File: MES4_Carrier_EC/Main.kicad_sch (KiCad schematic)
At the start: 20 parts, among them J1 2199230-3, J2 STDC14, SW1 RESET

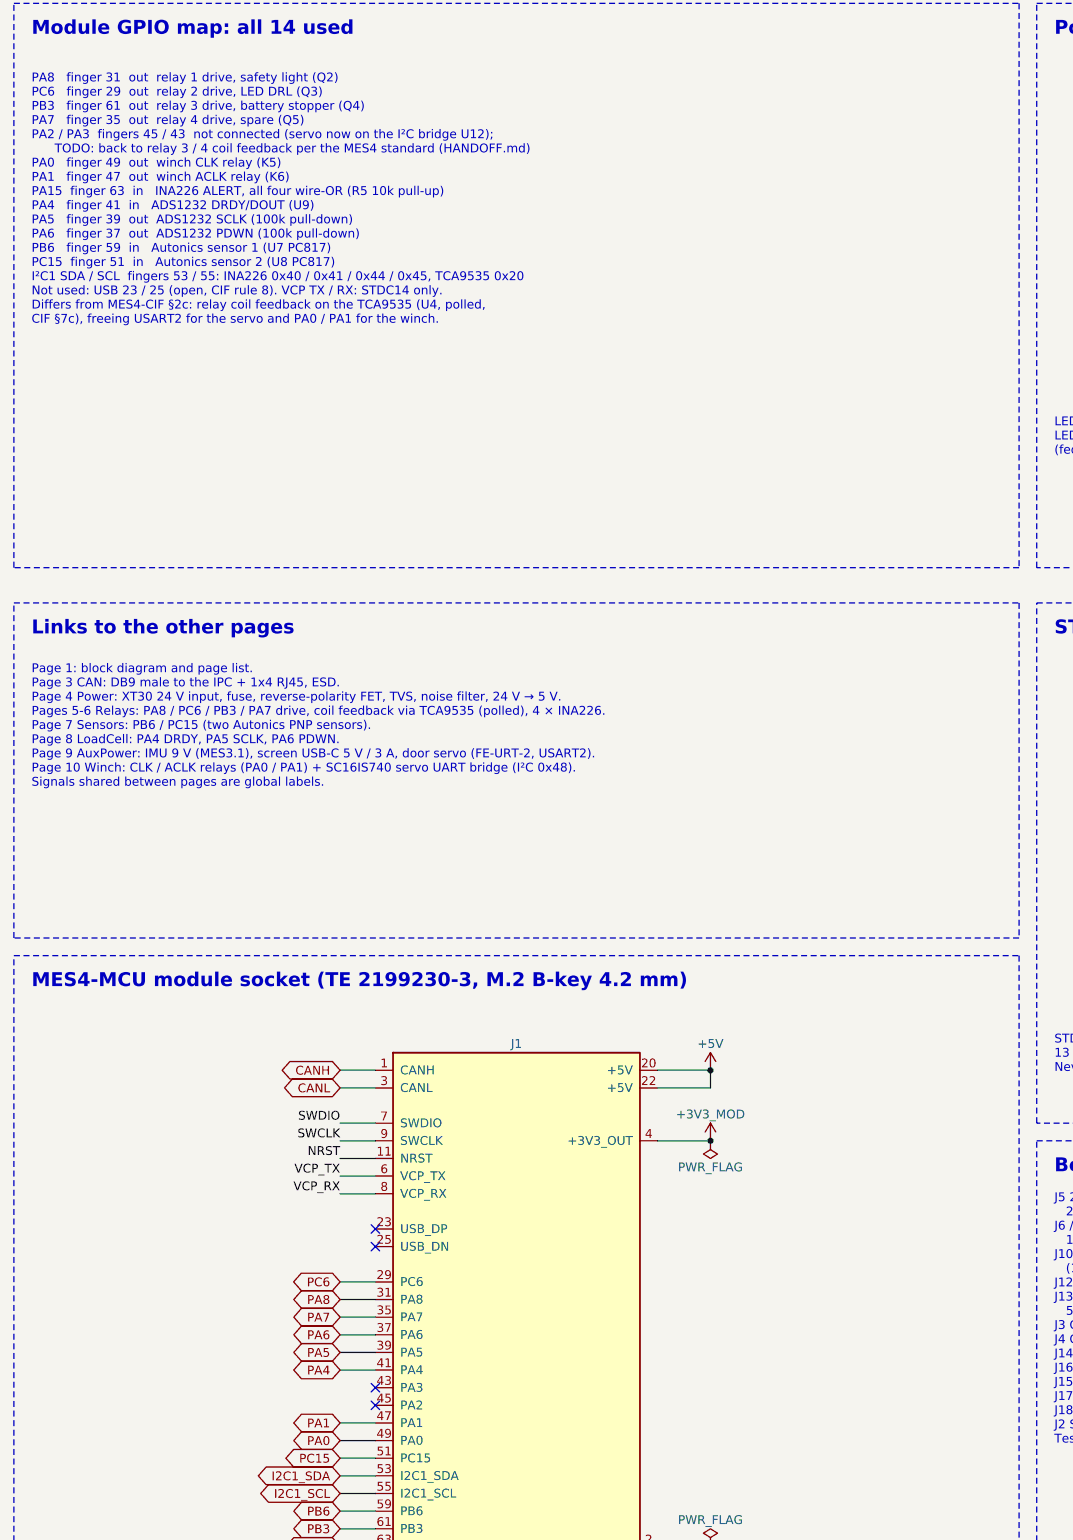
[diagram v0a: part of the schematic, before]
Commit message: Put relay coil feedback back on PA0-PA3 (MES4 GPIO standard)
All 14 module GPIOs now follow the MES4-CIF §2c table. The TCA9535 is
removed from the Relays 3-4 sheet and J1 fingers 43/45/47/49 drive the
relay 1-4 feedback dividers again. The winch relays are left undriven
(gate inputs no-connected, 100k pull-downs hold them off) until they
move to the TCA9535 + photoMOS design (HANDOFF.md step 2).

Removing U4 renumbers U5-U12 to U4-U11 and C15-C45 to C14-C44; the
README refs follow. Adds generator/checks.py (pin/pad, single-pin nets,
duplicate UUIDs, LCSC numbers), run by run.sh after ERC.

Co-Authored-By: Claude Opus 5.5 <noreply@anthropic.com>
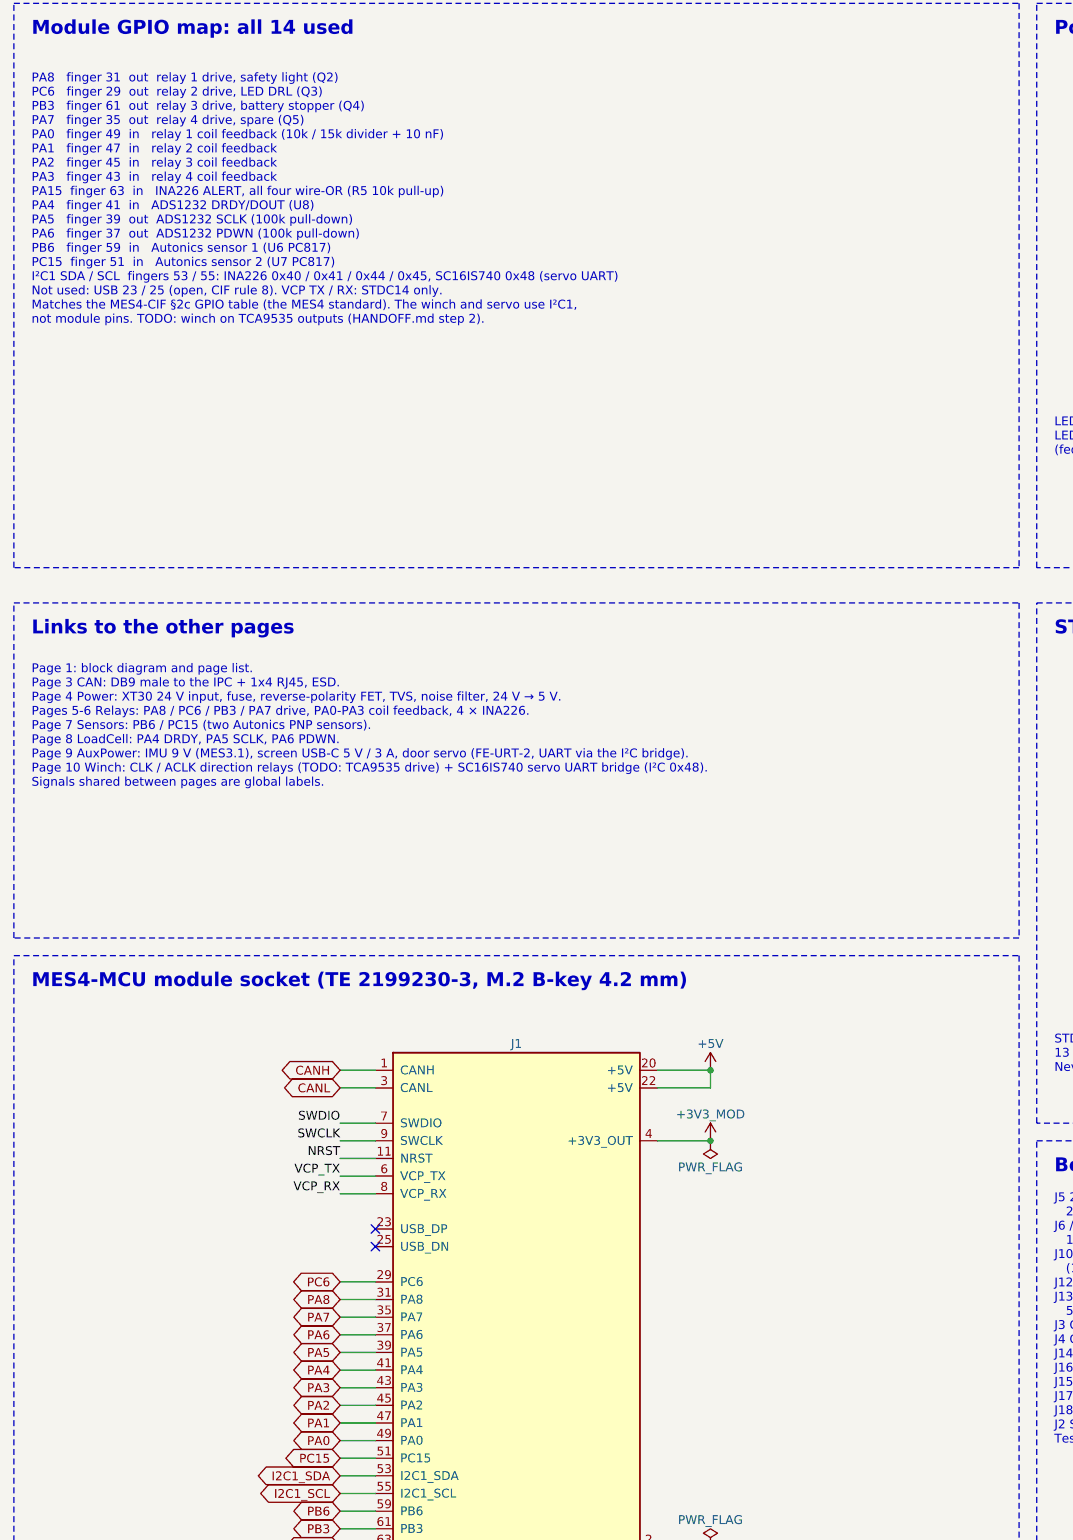
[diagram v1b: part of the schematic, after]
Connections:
- net PA3: now reaches J1.43 (PA3)
- net PA2: now reaches J1.45 (PA2)
- no-connect marks 9 -> 7
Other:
- note added: "PA8 finger 31 out relay 1 drive, safety light (Q2) PC6 finger 29 out relay 2 drive, LED DRL (Q3) PB3 finger 61 out relay 3 drive, battery stopper (Q4) PA7 finger 35 out relay 4 drive, spare (Q5) PA0 finger 49 in relay 1 coil feedback (10k / 15k divider + 10 nF) PA1 finger 47 in relay 2 coil feedback PA2 finger 45 in relay 3 coil feedback PA3 finger 43 in relay 4 coil feedback PA15 finger 63 in IN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"
- note added: "Page 1: block diagram and page list. Page 3 CAN: DB9 male to the IPC + 1x4 RJ45, ESD. Page 4 Power: XT30 24 V input, fuse, reverse-polarity FET, TVS, noise filter, 24 V → 5 V. Pages 5-6 Relays: PA8 / PC6 / PB3 / PA7 drive, PA0-PA3 coil feedback, 4 × INA226. Page 7 Sensors: PB6 / PC15 (two Autonics PNP sensors). Page 8 LoadCell: PA4 DRDY, PA5 SCLK, PA6 PDWN. Page 9 AuxPower: IMU 9 V (MES3.1), scre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"
- note removed: "PA8 finger 31 out relay 1 drive, safety light (Q2) PC6 finger 29 out relay 2 drive, LED DRL (Q3) PB3 finger 61 out relay 3 drive, battery stopper (Q4) PA7 finger 35 out relay 4 drive, spare (Q5) PA2 / PA3 fingers 45 / 43 not connected (servo now on the I²C bridge U12); TODO: back to relay 3 / 4 coil feedback per the MES4 standard (HANDOFF.md) PA0 finger 49 out winch CLK relay (K5) PA1 finger 47 o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"
- note removed: "Page 1: block diagram and page list. Page 3 CAN: DB9 male to the IPC + 1x4 RJ45, ESD. Page 4 Power: XT30 24 V input, fuse, reverse-polarity FET, TVS, noise filter, 24 V → 5 V. Pages 5-6 Relays: PA8 / PC6 / PB3 / PA7 drive, coil feedback via TCA9535 (polled), 4 × INA226. Page 7 Sensors: PB6 / PC15 (two Autonics PNP sensors). Page 8 LoadCell: PA4 DRDY, PA5 SCLK, PA6 PDWN. Page 9 AuxPower: IMU 9 V (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"

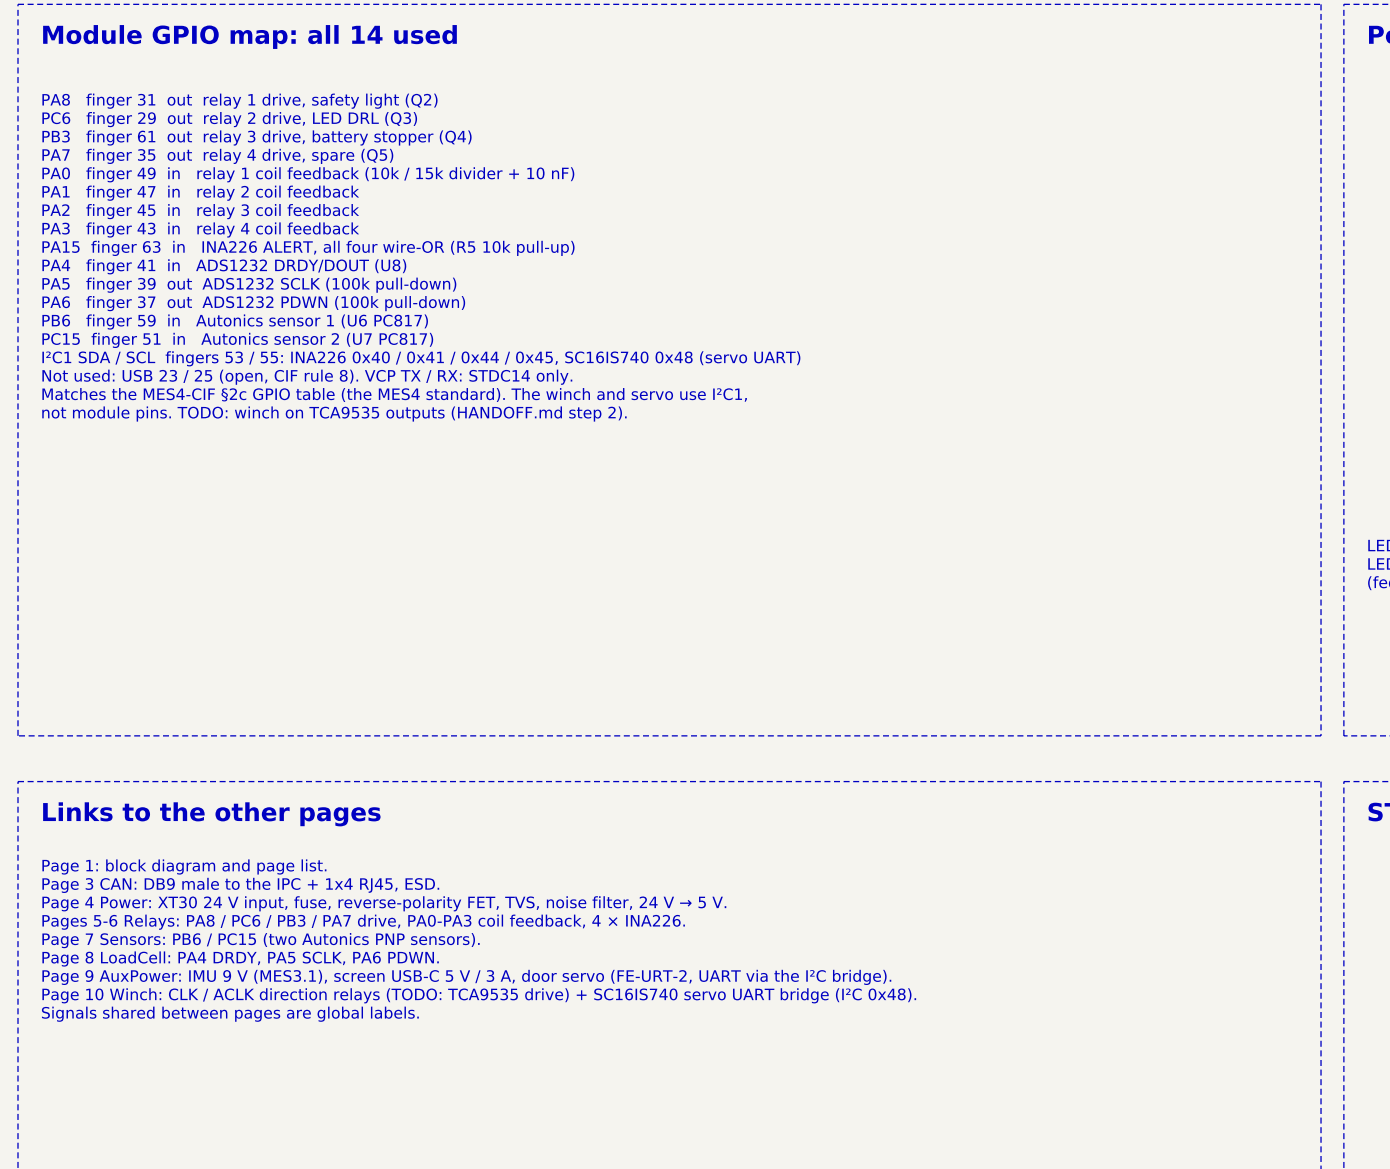
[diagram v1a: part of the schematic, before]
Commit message: Drop relay coil feedback; winch on PA0/PA1, servo on USART2
User decision: free the four feedback pins instead of adding an I²C
expander. The Flasher template's 10k/15k/10 nF dividers are removed from
all relay channels and relay diagnosis is INA226-only. PA0/PA1 drive the
IM03GR winch relays again and PA2/PA3 carry the door servo UART
(USART2), so the SC16IS740 bridge, its crystal and caps, and the unused
TCA9535 code are removed. This deliberately differs from the MES4-CIF
§2c GPIO table; the GPIO map, root notes, README and HANDOFF say so.

189 parts, ERC clean, checks.py passes. README refs follow the
renumbering.

Co-Authored-By: Claude Opus 5.5 <noreply@anthropic.com>
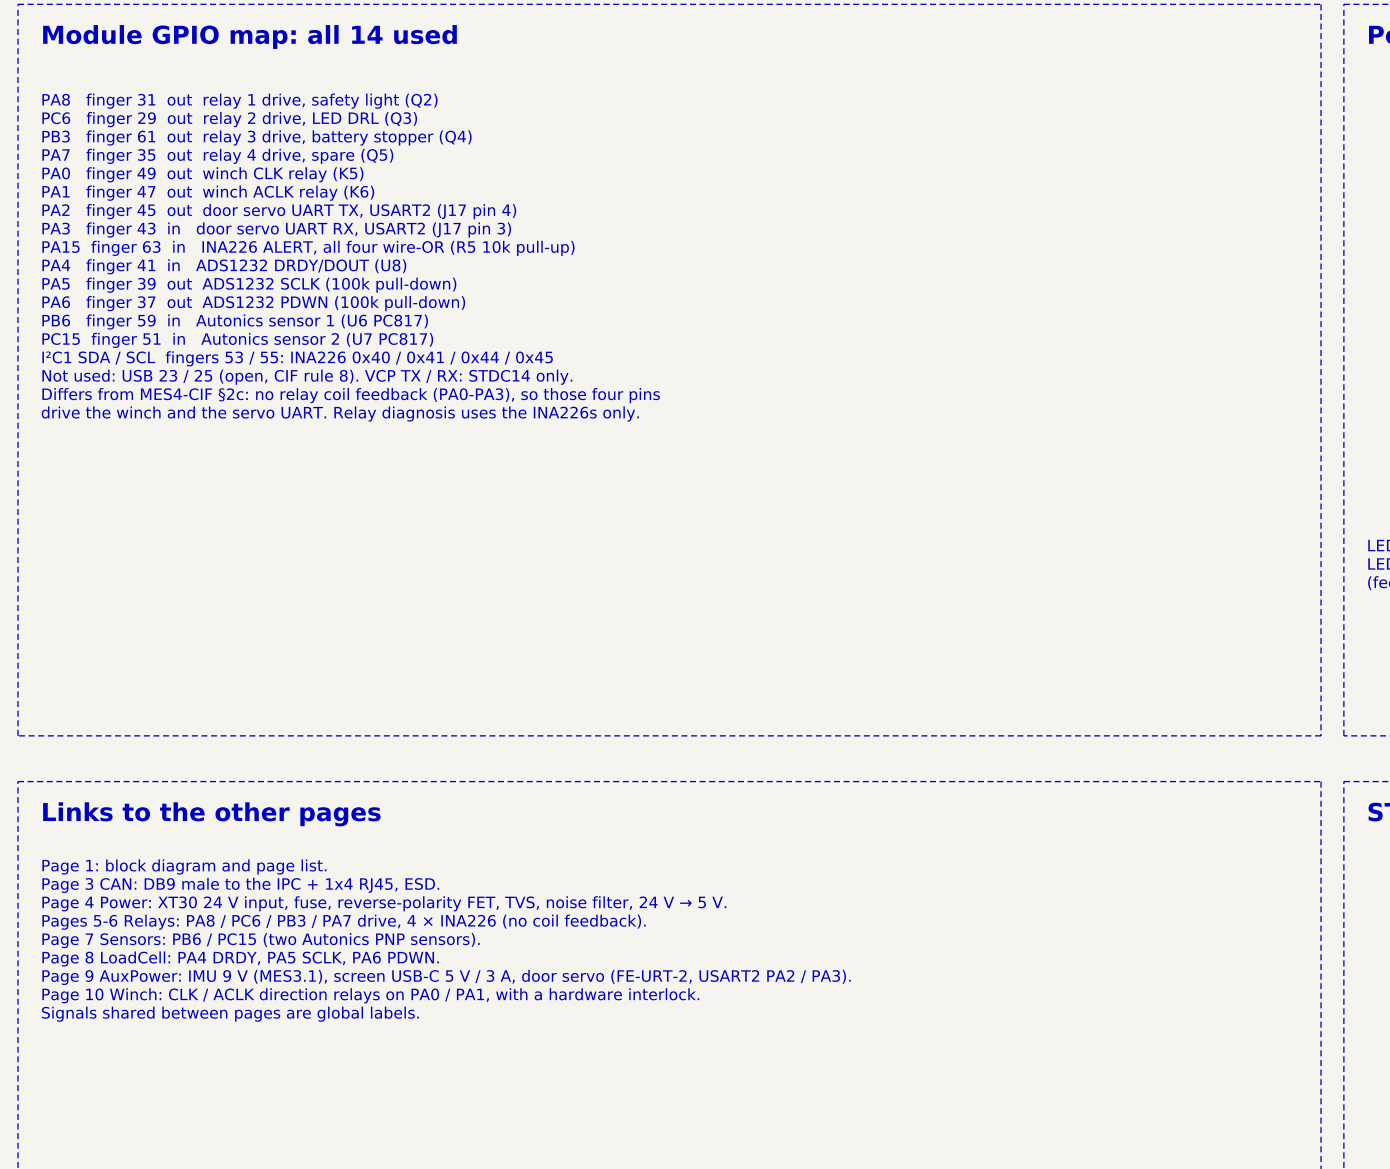
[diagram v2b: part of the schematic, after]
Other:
- note added: "PA8 finger 31 out relay 1 drive, safety light (Q2) PC6 finger 29 out relay 2 drive, LED DRL (Q3) PB3 finger 61 out relay 3 drive, battery stopper (Q4) PA7 finger 35 out relay 4 drive, spare (Q5) PA0 finger 49 out winch CLK relay (K5) PA1 finger 47 out winch ACLK relay (K6) PA2 finger 45 out door servo UART TX, USART2 (J17 pin 4) PA3 finger 43 in door servo UART RX, USART2 (J17 pin 3) PA15 finger 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"
- note added: "Page 1: block diagram and page list. Page 3 CAN: DB9 male to the IPC + 1x4 RJ45, ESD. Page 4 Power: XT30 24 V input, fuse, reverse-polarity FET, TVS, noise filter, 24 V → 5 V. Pages 5-6 Relays: PA8 / PC6 / PB3 / PA7 drive, 4 × INA226 (no coil feedback). Page 7 Sensors: PB6 / PC15 (two Autonics PNP sensors). Page 8 LoadCell: PA4 DRDY, PA5 SCLK, PA6 PDWN. Page 9 AuxPower: IMU 9 V (MES3.1), screen U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"
- note removed: "PA8 finger 31 out relay 1 drive, safety light (Q2) PC6 finger 29 out relay 2 drive, LED DRL (Q3) PB3 finger 61 out relay 3 drive, battery stopper (Q4) PA7 finger 35 out relay 4 drive, spare (Q5) PA0 finger 49 in relay 1 coil feedback (10k / 15k divider + 10 nF) PA1 finger 47 in relay 2 coil feedback PA2 finger 45 in relay 3 coil feedback PA3 finger 43 in relay 4 coil feedback PA15 finger 63 in IN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"
- note removed: "Page 1: block diagram and page list. Page 3 CAN: DB9 male to the IPC + 1x4 RJ45, ESD. Page 4 Power: XT30 24 V input, fuse, reverse-polarity FET, TVS, noise filter, 24 V → 5 V. Pages 5-6 Relays: PA8 / PC6 / PB3 / PA7 drive, PA0-PA3 coil feedback, 4 × INA226. Page 7 Sensors: PB6 / PC15 (two Autonics PNP sensors). Page 8 LoadCell: PA4 DRDY, PA5 SCLK, PA6 PDWN. Page 9 AuxPower: IMU 9 V (MES3.1), scre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"

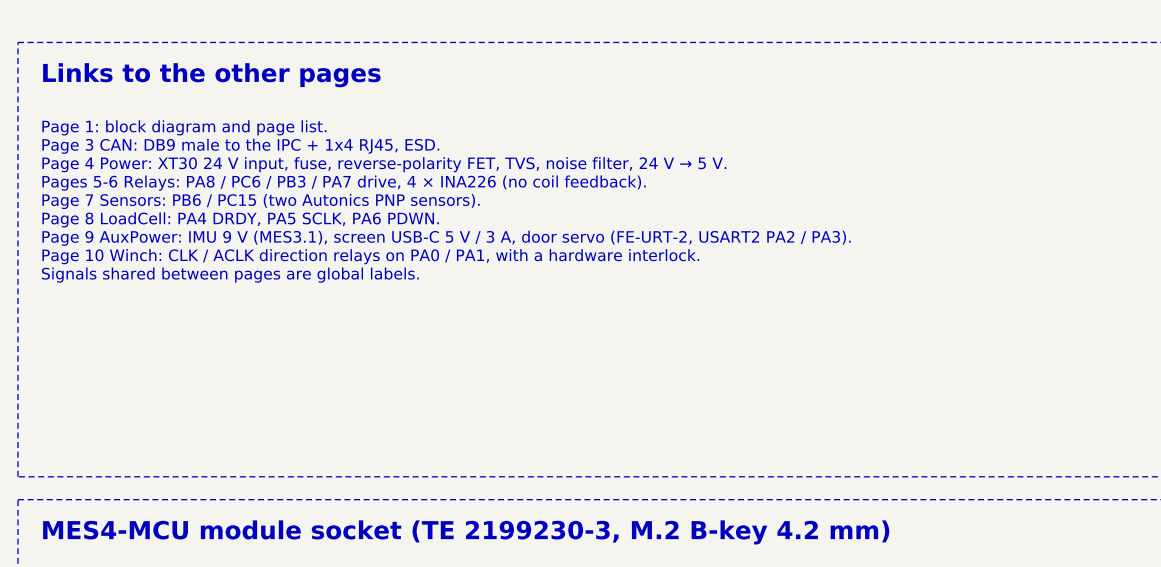
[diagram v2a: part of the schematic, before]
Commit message: Add module finger map page and FE-URT-2 3.3 V note
New page 11 (Pinout): a KiCad table of every MES4-MCU finger with its
STM32 port, function, what this carrier connects to it, the carrier
parts, the MES4-CIF §2c standard use and notes. It follows the MES4-MCU
U1 pin map style (colour-coded Function column, spanned finger-group
rows); the PA0-PA3 rows mark where this board differs from §2c. The
builder gains table() with per-cell fills and row spans, and cell text
resolves {tag} references.

The AuxPower servo note, README and HANDOFF now say to set the FE-URT-2
level switch to 3.3 V: at 5 V its TX exceeds PA3's limit while the
module is unpowered and back-feeds the 3V3 through the RX pull-up.

Co-Authored-By: Claude Opus 5.5 <noreply@anthropic.com>
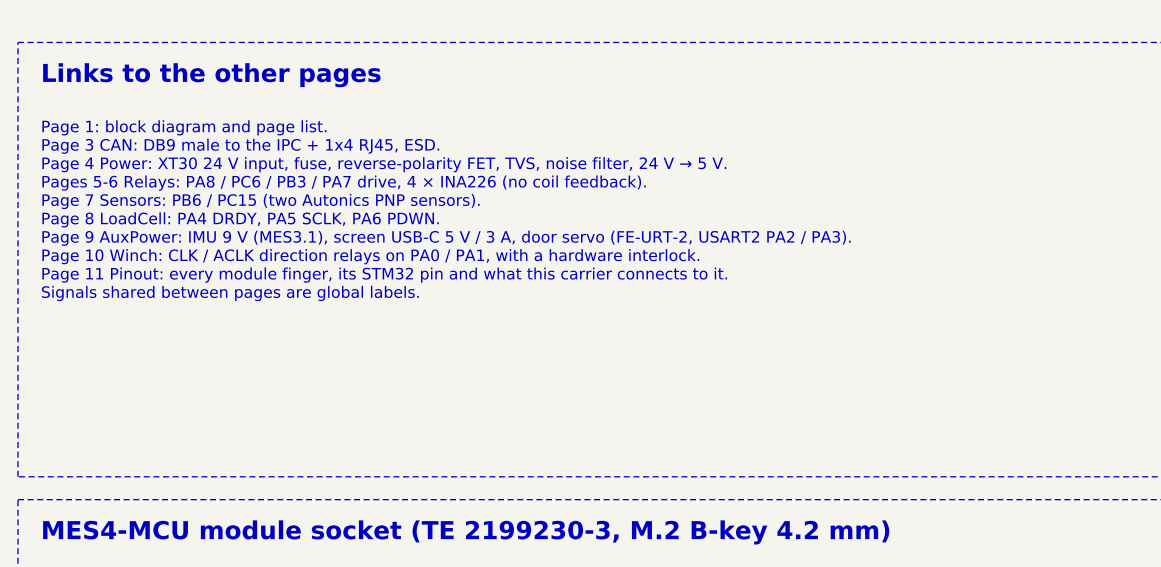
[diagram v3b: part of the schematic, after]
